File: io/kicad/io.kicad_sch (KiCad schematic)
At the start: 52 parts, among them J1 Conn_01x04_Pin, J2 Conn_01x04_Pin, J3 pcie_98, U1 B0505MT-1WR4, U2 ESD5344D-TP, U3 ESD5344D-TP, U4 ADUM1201ARZ-RL7, U5 ADUM1201ARZ-RL7, U6 XC6206P332MR, U7 XC6206P332MR, U8 ESD5344D-TP

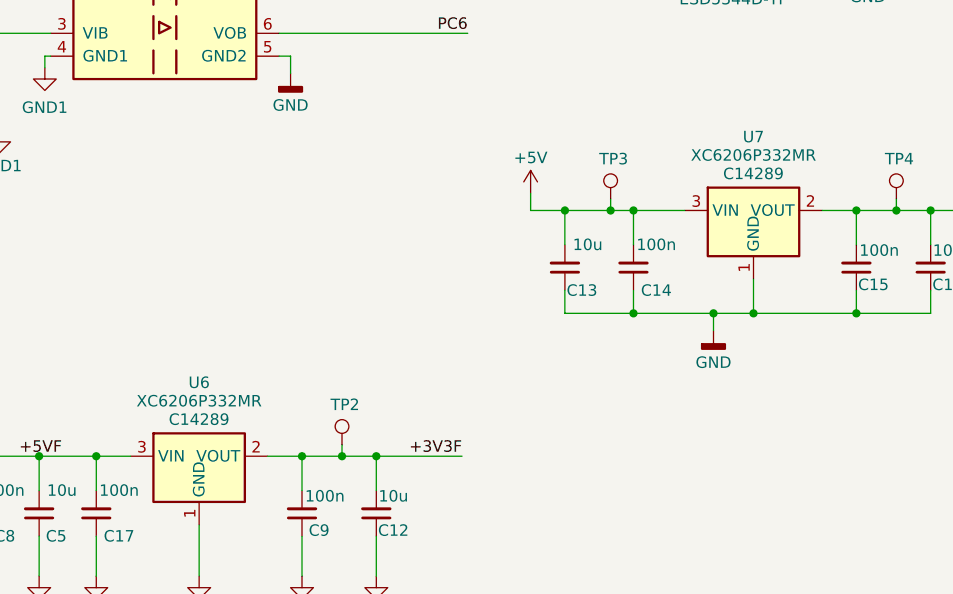
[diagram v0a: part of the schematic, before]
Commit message: Fixed the part numbers and footpring of the IO board's 3.3V regulators.
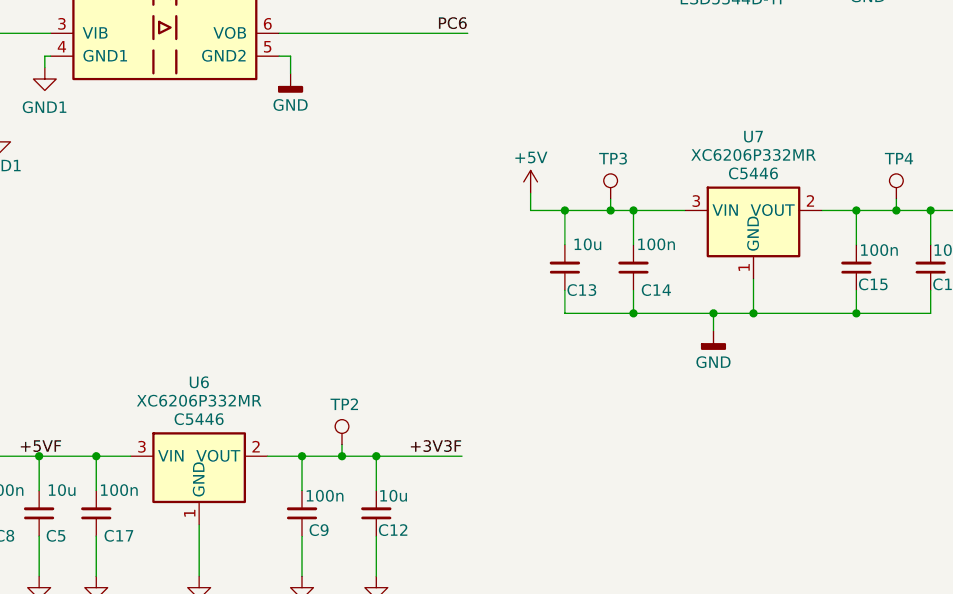
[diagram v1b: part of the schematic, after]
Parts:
- U6, U7: footprint Package_TO_SOT_SMD:SOT-89-3 -> Package_TO_SOT_SMD:SOT-23-3; LCSC C14289 -> C5446
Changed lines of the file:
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@@
       (effects (font (size 1.27 1.27)))
     )
-    (property "Footprint" "Package_TO_SOT_SMD:SOT-89-3" (at 105.41 163.83 0)
+    (property "Footprint" "Package_TO_SOT_SMD:SOT-23-3" (at 105.41 163.83 0)
       (effects (font (size 1.27 1.27) italic) hide)
     )
@@
       (effects (font (size 1.27 1.27)) hide)
     )
-    (property "LCSC" "C14289" (at 105.41 165.473 0)
+    (property "LCSC" "C5446" (at 105.41 165.473 0)
       (effects (font (size 1.27 1.27)))
     )
@@
       (effects (font (size 1.27 1.27)))
     )
-    (property "Footprint" "Package_TO_SOT_SMD:SOT-89-3" (at 167.005 136.525 0)
+    (property "Footprint" "Package_TO_SOT_SMD:SOT-23-3" (at 167.005 136.525 0)
       (effects (font (size 1.27 1.27) italic) hide)
     )
@@
       (effects (font (size 1.27 1.27)) hide)
     )
-    (property "LCSC" "C14289" (at 167.005 138.168 0)
-      (effects (font (size 1.27 1.27)))
-    )
+    (property "LCSC" "C5446" (at 167.005 138.168 0)
+      (effects (font (size 1.27 1.27)))
+    )

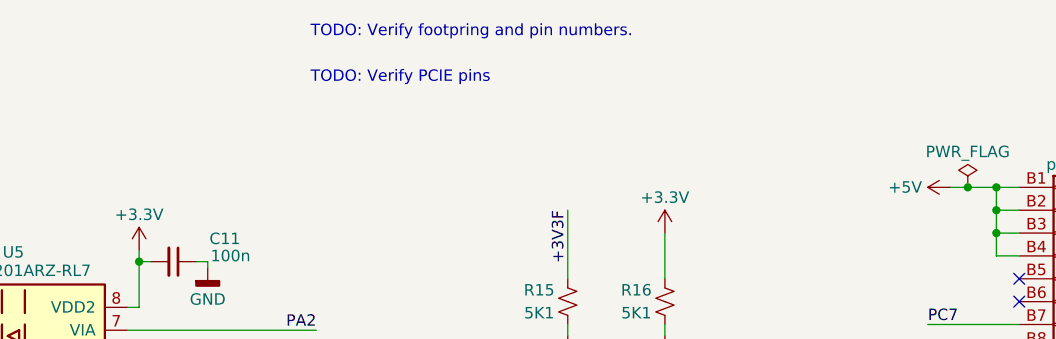
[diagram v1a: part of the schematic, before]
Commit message: Added TODOs to Kicad schematics.
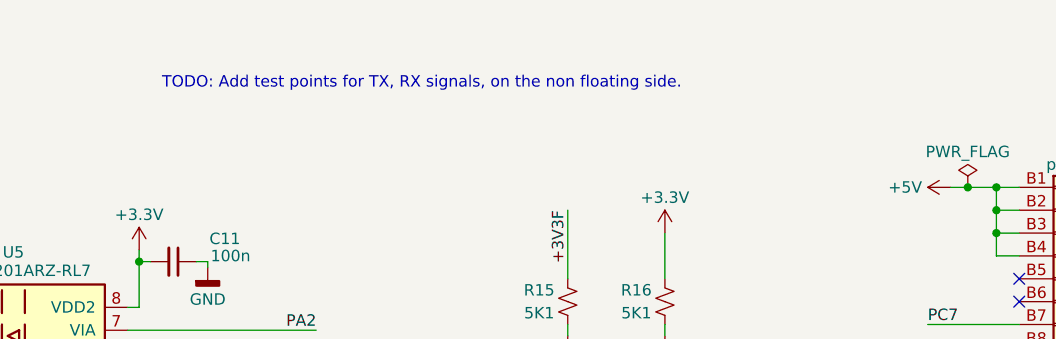
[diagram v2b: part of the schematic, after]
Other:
- note added: "TODO: Add test points for TX, RX signals, on the non floating side."
- note removed: "TODO: Verify PCIE pins"
- note removed: "TODO: Verify footpring and pin numbers."
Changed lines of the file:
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@@
     (effects (font (size 1.27 1.27)) (justify left bottom))
   )
-  (text "TODO: Verify footpring and pin numbers." (at 136.525 17.78 0)
+  (text "TODO: Add test points for TX, RX signals, on the non floating side."
+    (at 120.015 23.495 0)
     (effects (font (size 1.27 1.27) (color 255 0 0 1)) (justify left bottom))
   )
@@
     (effects (font (size 1.27 1.27)) (justify left bottom))
   )
-  (text "TODO: Verify PCIE pins" (at 136.525 22.86 0)
-    (effects (font (size 1.27 1.27) (color 255 0 0 1)) (justify left bottom))
-  )
   (text "SERIAL" (at 20.32 56.515 0)

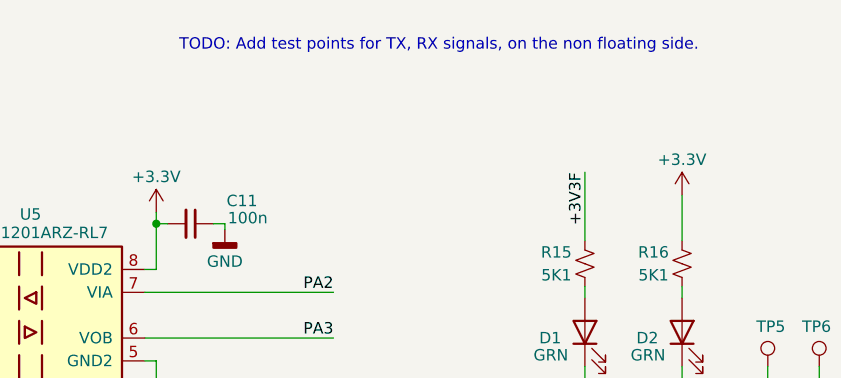
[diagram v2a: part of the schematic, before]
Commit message: Added TODOs to kicad schematics (adding a serial number silkscreen)
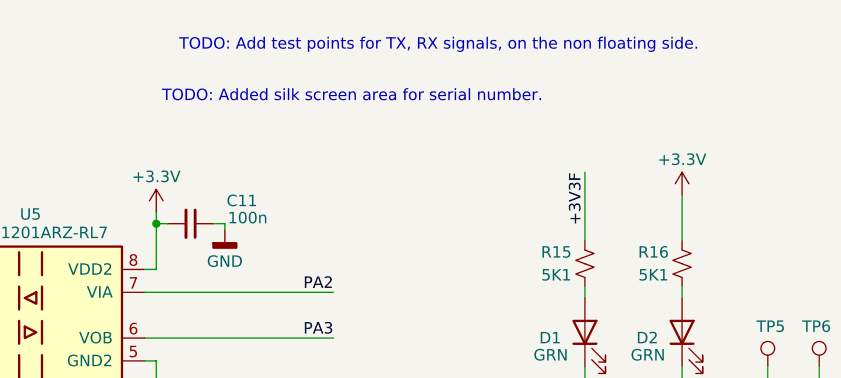
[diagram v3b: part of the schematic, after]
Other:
- note added: "TODO: Added silk screen area for serial number."
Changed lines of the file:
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@@
     (effects (font (size 1.27 1.27)) (justify left bottom))
+  )
+  (text "TODO: Added silk screen area for serial number." (at 118.11 29.21 0)
+    (effects (font (size 1.27 1.27) (color 255 0 0 1)) (justify left bottom))
   )
   (text "DIGITAL" (at 17.145 123.825 0)

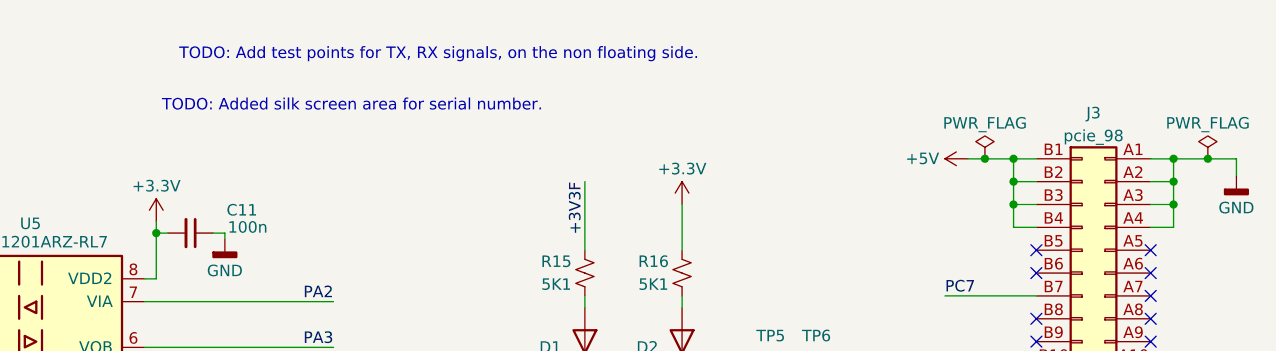
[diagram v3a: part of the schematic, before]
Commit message: Routed V2 of the heater board.
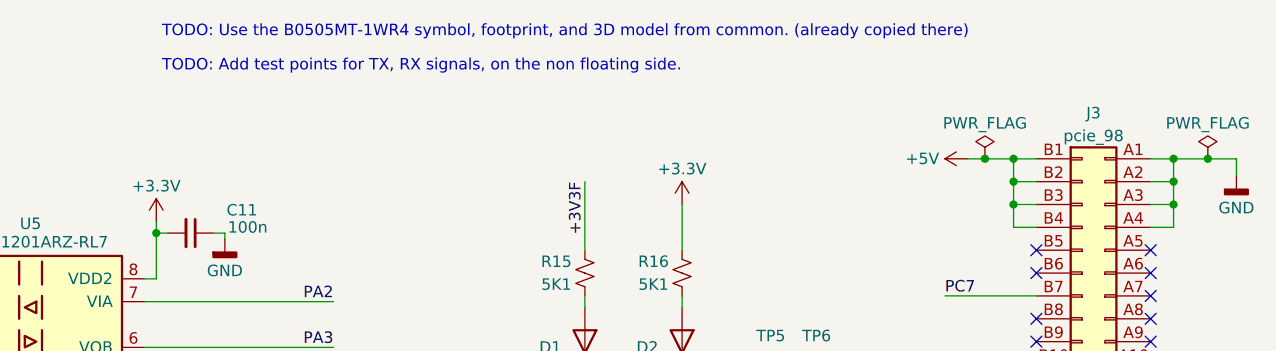
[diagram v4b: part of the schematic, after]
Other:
- note added: "TODO: Use the B0505MT-1WR4 symbol, footprint, and 3D model from common. (already copied there)"
- note removed: "TODO: Added silk screen area for serial number."
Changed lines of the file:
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@@
     (effects (font (size 1.27 1.27)) (justify left bottom))
-  )
-  (text "TODO: Added silk screen area for serial number." (at 118.11 29.21 0)
-    (effects (font (size 1.27 1.27) (color 255 0 0 1)) (justify left bottom))
   )
   (text "DIGITAL" (at 17.145 123.825 0)
@@
   )
   (text "TODO: Add test points for TX, RX signals, on the non floating side."
-    (at 120.015 23.495 0)
+    (at 118.11 24.765 0)
     (effects (font (size 1.27 1.27) (color 255 0 0 1)) (justify left bottom))
   )
@@
     (effects (font (size 1.27 1.27)) (justify left bottom))
   )
+  (text "TODO: Use the B0505MT-1WR4 symbol, footprint, and 3D model from common. (already copied there)"
+    (at 118.11 20.955 0)
+    (effects (font (size 1.27 1.27) (color 255 0 0 1)) (justify left bottom))
+  )
   (text "GND" (at 29.21 59.055 0)
